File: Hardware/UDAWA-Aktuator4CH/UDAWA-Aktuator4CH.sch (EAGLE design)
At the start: 3 parts

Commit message: #3 to do list 1 sampai 5
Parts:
- added 5V, AC/DC1, AC/DC2, AC/DC3, AC/DC4, C1, C2, C3, C4, CH1, CH2, CH3, CH4, GND, NO1, NO3, RC1, RC2, RC3, RC4: (no value), con-wago-500:W237-102
- added F1, F2, F3, F4: (no value), fuse:19559
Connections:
- new net AC/DC1: AC/DC1-1.KL, CH1-2.KL
- new net AC/DC2: AC/DC2-1.KL, CH2-2.KL
- new net AC/DC3: AC/DC3-1.KL, CH3-2.KL
- new net AC/DC4: AC/DC4-1.KL, CH4-2.KL
- new net C1: C1-1.KL, U$1.IO27
- new net C2: C2-1.KL, U$1.IO26
- new net C3: C3-1.KL, U$1.IO25
- new net C4: C4-1.KL, U$1.IO33
- new net GND2: GND-1.KL, U$1.GND@2
- new net N$1: F1.2, RC1-2.KL
- new net N$3: F2.2, RC2-2.KL
- new net N$5: F3.2, RC3-2.KL
- new net N$7: F4.2, RC4-2.KL
- new net NO1: CH1-1.KL, NO1-1.KL
- new net NO2: CH2-1.KL, NO1-2.KL
- new net NO3: CH3-1.KL, NO3-1.KL
- new net NO4: CH4-1.KL, NO3-2.KL
- new net RC1: AC/DC1-2.KL, F1.1
- new net RC2: AC/DC2-2.KL, F2.1
- new net RC3: AC/DC3-2.KL, F3.1
- new net RC4: AC/DC4-2.KL, F4.1

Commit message: #3 perbaikan to do list 1sampai5
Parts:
- removed 5V, AC/DC2, AC/DC3, AC/DC4, C3, C4, RC3, RC4: (no value), con-wago-500:W237-102
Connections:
- removed net N$5: F3.2, RC3-2.KL
- removed net N$7: F4.2, RC4-2.KL
- removed net RC1: AC/DC1-2.KL, F1.1
- removed net RC2: AC/DC2-2.KL, F2.1
- removed net RC3: AC/DC3-2.KL, F3.1
- removed net RC4: AC/DC4-2.KL, F4.1
- new net -R1: AC/DC1-1.KL
- new net N$2: F2.2, RC1-1.KL
- new net N$4: F4.2, RC2-1.KL
- new net VCC: GND-2.KL, U$1.3V3
- new net ~R1: AC/DC1-2.KL, F1.1, F2.1, F3.1, F4.1
- net AC/DC1: no longer AC/DC1-1.KL
- net AC/DC2: no longer AC/DC2-1.KL
- net AC/DC3: no longer AC/DC3-1.KL
- net AC/DC4: no longer AC/DC4-1.KL
- net C2: now also C1-2.KL; no longer C2-1.KL
- net C3: now also C2-1.KL; no longer C3-1.KL
- net C4: now also C2-2.KL; no longer C4-1.KL
- net N$3: now also F3.2; no longer F2.2
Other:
- moved on the sheet: F1, F2, F3, F4

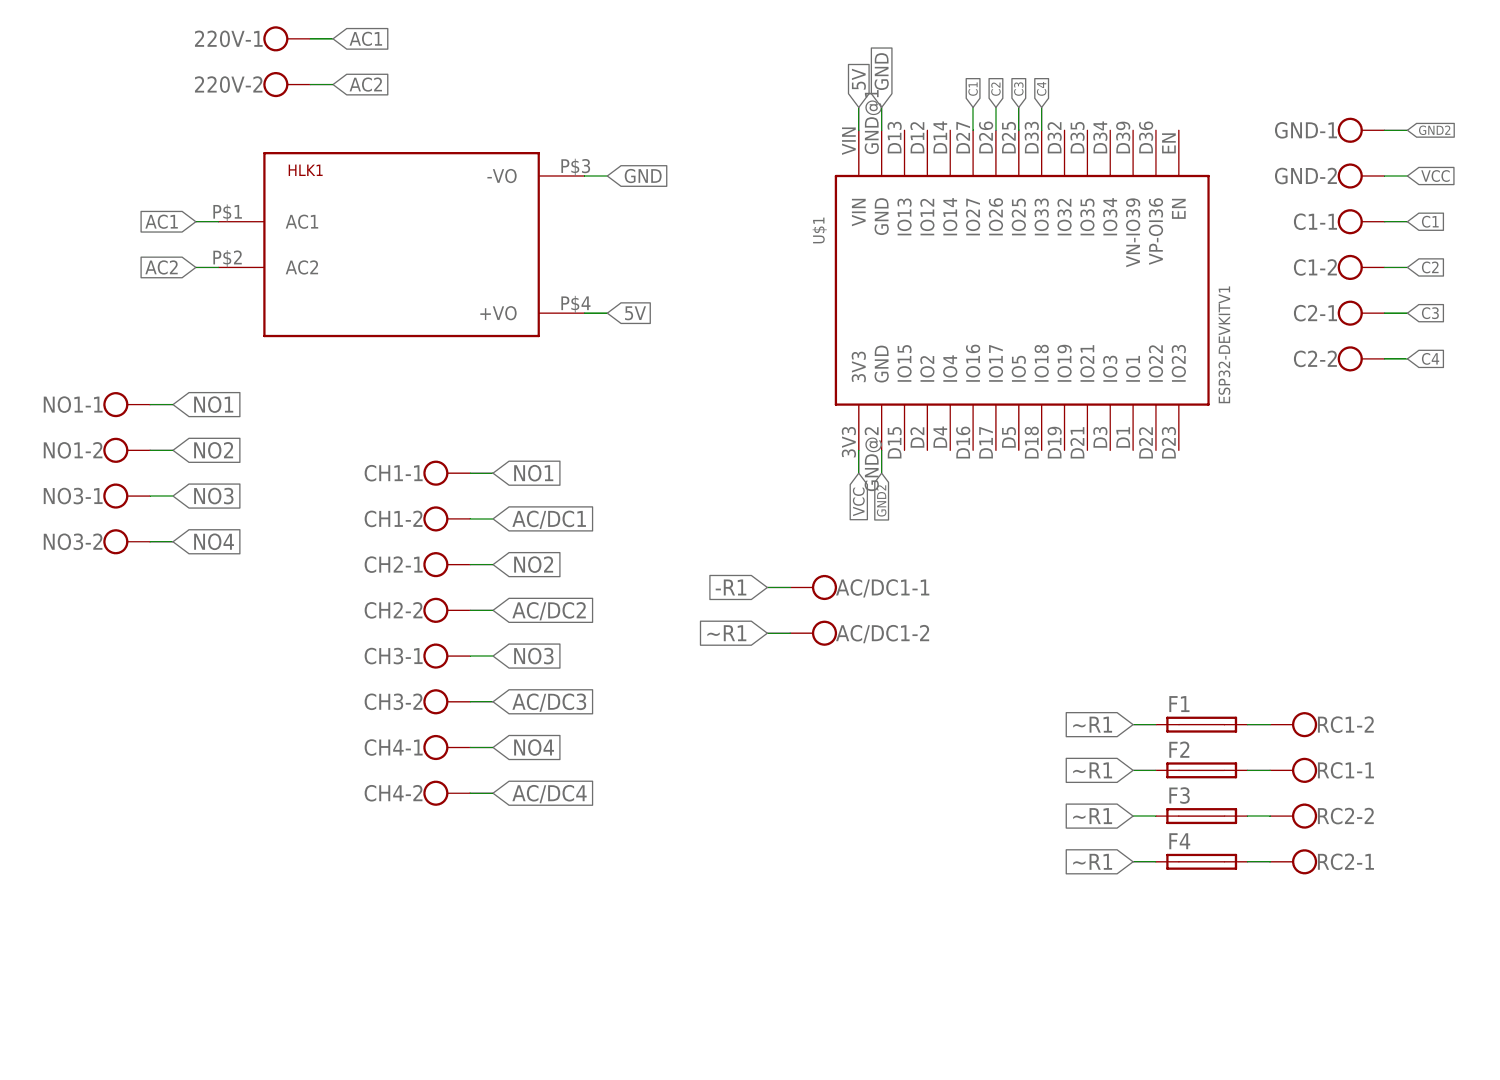
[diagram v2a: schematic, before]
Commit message: #3 wiring pada mode board dan pastikan penamaan setiap pin dan konektor dibuat dengan jelas dan rapi sesuai diagram.
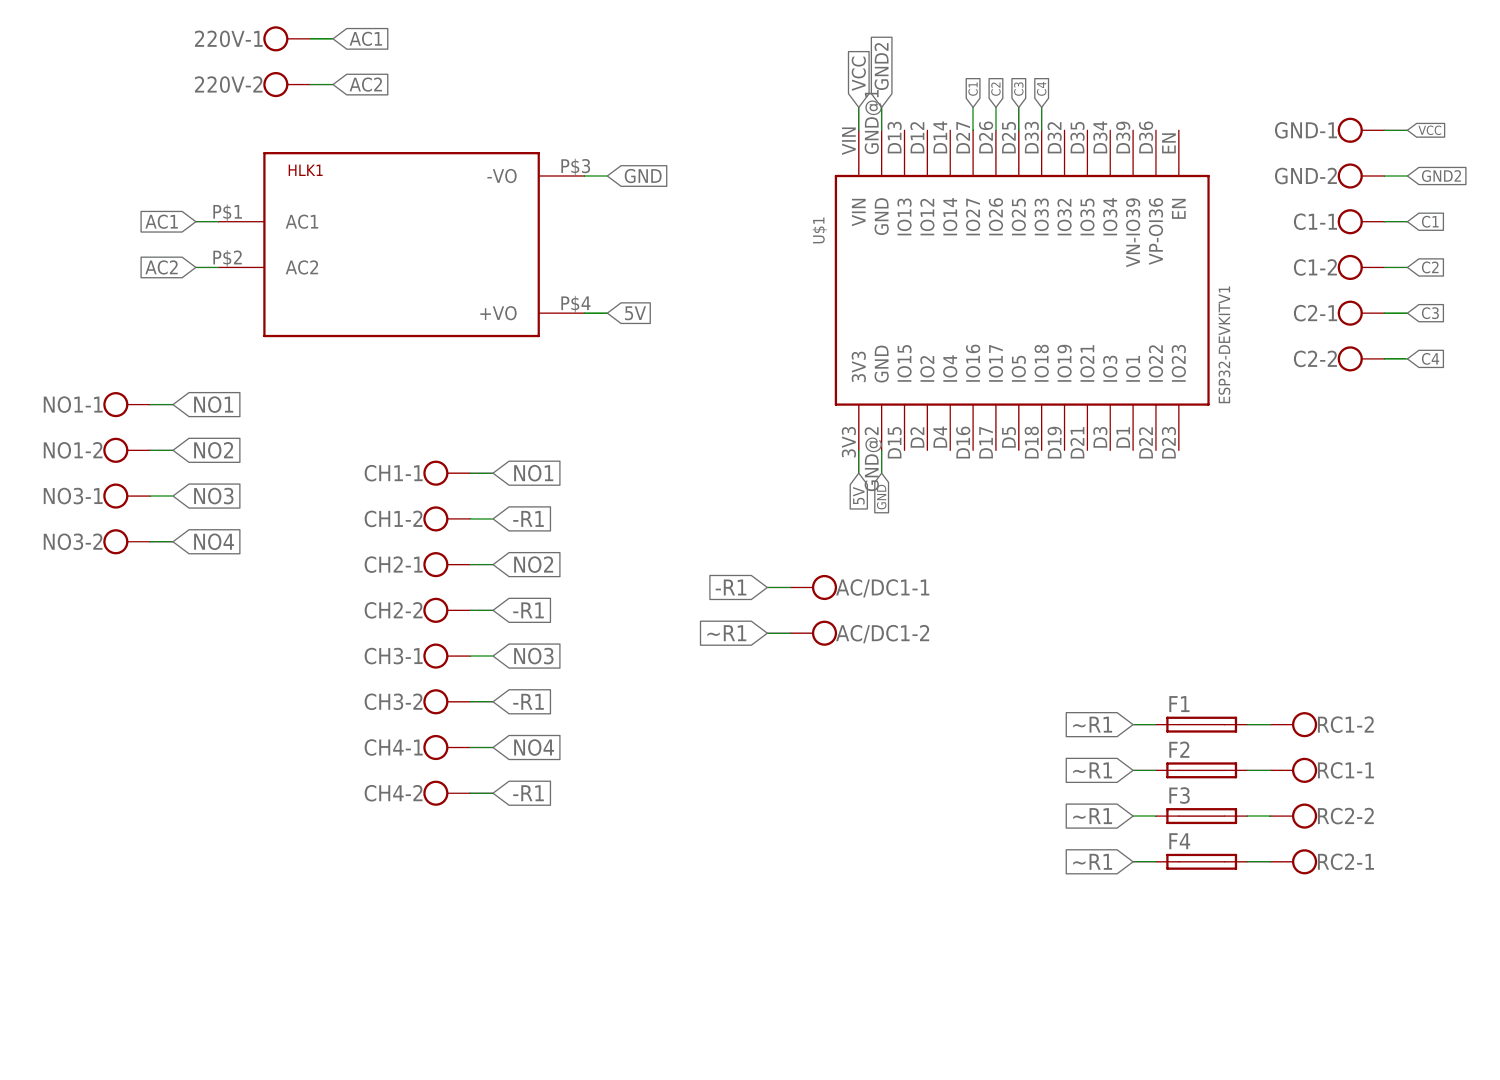
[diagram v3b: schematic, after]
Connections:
- removed net AC/DC1: CH1-2.KL
- removed net AC/DC2: CH2-2.KL
- removed net AC/DC3: CH3-2.KL
- removed net AC/DC4: CH4-2.KL
- net -R1: now also CH1-2.KL, CH2-2.KL, CH3-2.KL, CH4-2.KL
- net 5V: now also U$1.3V3; no longer U$1.VIN
- net GND: now also U$1.GND@2; no longer U$1.GND@1
- net GND2: now also GND-2.KL, U$1.GND@1; no longer GND-1.KL, U$1.GND@2
- net VCC: now also GND-1.KL, U$1.VIN; no longer GND-2.KL, U$1.3V3

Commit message: #3 list 8
masih belum lengkap  wiringnya karena kabelnya sudah mentok dan bakalan numpuk kalau dipaksakan
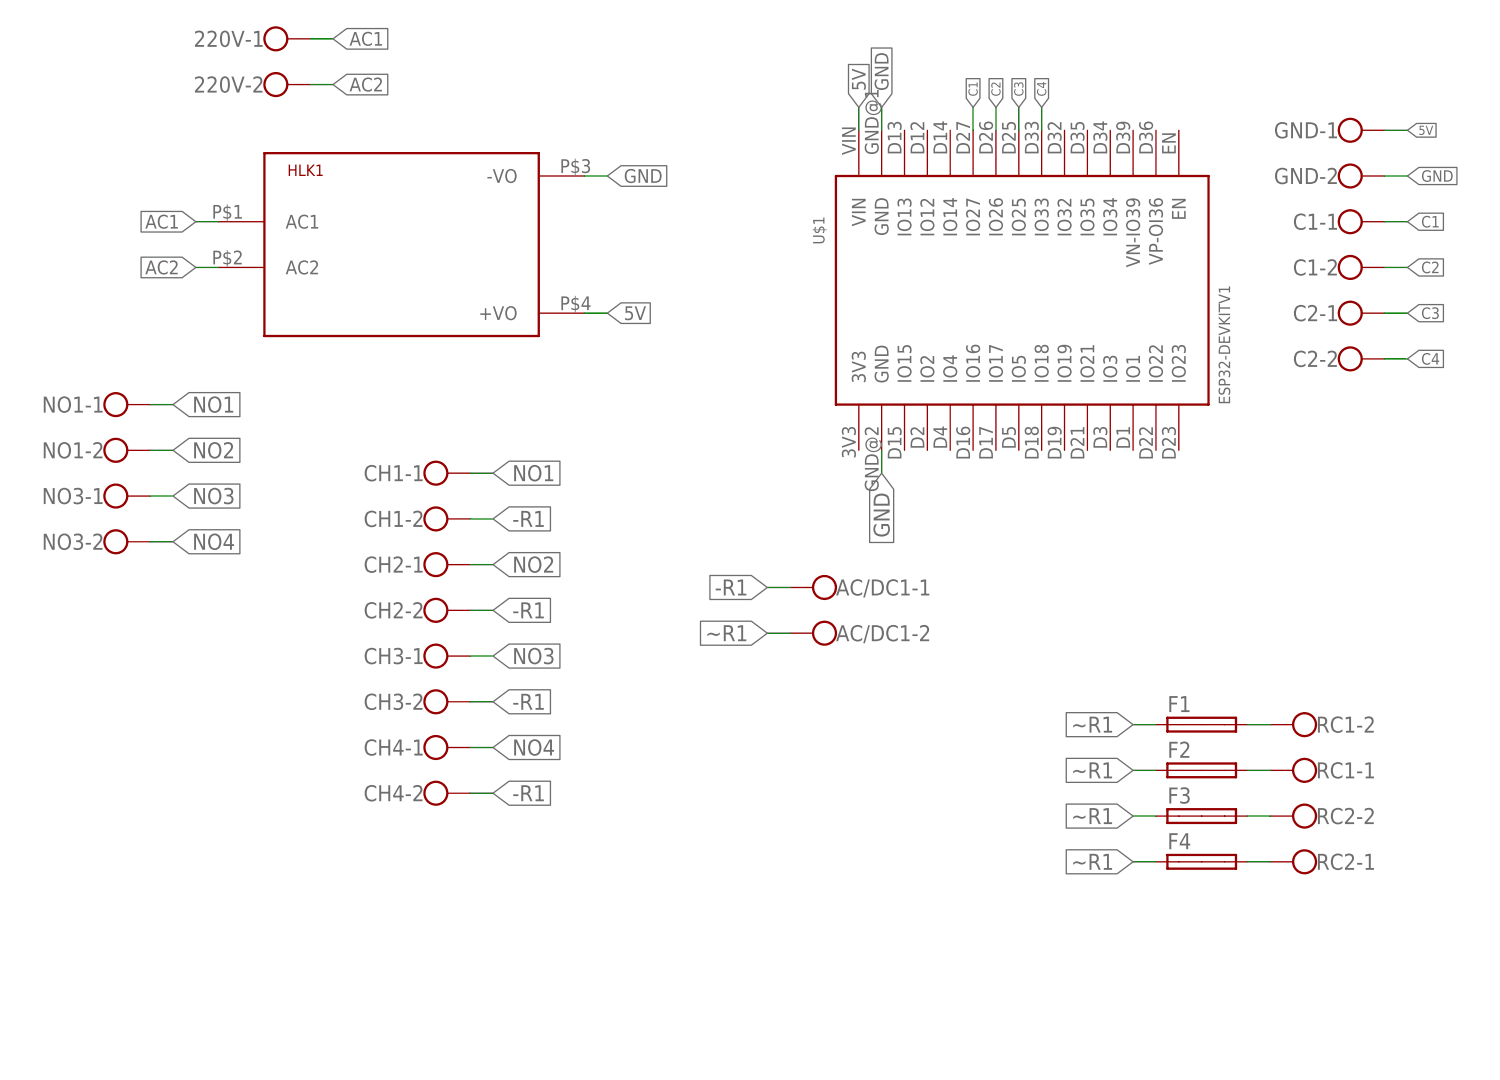
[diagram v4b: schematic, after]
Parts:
- F1, F2, F3, F4: device fuse:19559 -> fuse:SHK20L
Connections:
- removed net GND2: GND-2.KL, U$1.GND@1
- removed net VCC: GND-1.KL, U$1.VIN
- net 5V: now also GND-1.KL, U$1.VIN; no longer U$1.3V3
- net GND: now also GND-2.KL, U$1.GND@1
- net N$1: now also F1.2A; no longer F1.2
- net N$2: now also F2.2A; no longer F2.2
- net N$3: now also F3.2A; no longer F3.2
- net N$4: now also F4.2A; no longer F4.2
- net ~R1: now also F1.1A, F2.1A, F3.1A, F4.1A; no longer F1.1, F2.1, F3.1, F4.1
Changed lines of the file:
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@@
 <part name="RC1" library="con-wago-500" library_urn="urn:adsk.eagle:library:195" deviceset="W237-102" device="" package3d_urn="urn:adsk.eagle:package:10688/1"/>
 <part name="RC2" library="con-wago-500" library_urn="urn:adsk.eagle:library:195" deviceset="W237-102" device="" package3d_urn="urn:adsk.eagle:package:10688/1"/>
-<part name="F1" library="fuse" library_urn="urn:adsk.eagle:library:233" deviceset="19559" device="" package3d_urn="urn:adsk.eagle:package:14056/1"/>
-<part name="F2" library="fuse" library_urn="urn:adsk.eagle:library:233" deviceset="19559" device="" package3d_urn="urn:adsk.eagle:package:14056/1"/>
-<part name="F3" library="fuse" library_urn="urn:adsk.eagle:library:233" deviceset="19559" device="" package3d_urn="urn:adsk.eagle:package:14056/1"/>
-<part name="F4" library="fuse" library_urn="urn:adsk.eagle:library:233" deviceset="19559" device="" package3d_urn="urn:adsk.eagle:package:14056/1"/>
+<part name="F1" library="fuse" library_urn="urn:adsk.eagle:library:233" deviceset="SHK20L" device="" package3d_urn="urn:adsk.eagle:package:14071/1"/>
+<part name="F2" library="fuse" library_urn="urn:adsk.eagle:library:233" deviceset="SHK20L" device="" package3d_urn="urn:adsk.eagle:package:14071/1"/>
+<part name="F3" library="fuse" library_urn="urn:adsk.eagle:library:233" deviceset="SHK20L" device="" package3d_urn="urn:adsk.eagle:package:14071/1"/>
+<part name="F4" library="fuse" library_urn="urn:adsk.eagle:library:233" deviceset="SHK20L" device="" package3d_urn="urn:adsk.eagle:package:14071/1"/>
 </parts>
 <sheets>
@@
 <attribute name="NAME" x="73.66" y="-61.849" size="1.778" layer="95"/>
 </instance>
-<instance part="F1" gate="1" x="60.96" y="-50.8" smashed="yes">
+<instance part="F1" gate="G$1" x="60.96" y="-50.8" smashed="yes">
 <attribute name="NAME" x="57.15" y="-49.403" size="1.778" layer="95"/>
 <attribute name="VALUE" x="57.15" y="-53.721" size="1.778" layer="96"/>
 </instance>
-<instance part="F2" gate="1" x="60.96" y="-55.88" smashed="yes">
+<instance part="F2" gate="G$1" x="60.96" y="-55.88" smashed="yes">
 <attribute name="NAME" x="57.15" y="-54.483" size="1.778" layer="95"/>
 <attribute name="VALUE" x="57.15" y="-58.801" size="1.778" layer="96"/>
 </instance>
-<instance part="F3" gate="1" x="60.96" y="-60.96" smashed="yes">
+<instance part="F3" gate="G$1" x="60.96" y="-60.96" smashed="yes">
 <attribute name="NAME" x="57.15" y="-59.563" size="1.778" layer="95"/>
 <attribute name="VALUE" x="57.15" y="-63.881" size="1.778" layer="96"/>
 </instance>
-<instance part="F4" gate="1" x="60.96" y="-66.04" smashed="yes">
+<instance part="F4" gate="G$1" x="60.96" y="-66.04" smashed="yes">
 <attribute name="NAME" x="57.15" y="-64.643" size="1.778" layer="95"/>
 <attribute name="VALUE" x="57.15" y="-68.961" size="1.778" layer="96"/>
@@
 </segment>
 <segment>
+<pinref part="U$1" gate="G$1" pin="GND@1"/>
+<wire x1="25.4" y1="15.24" x2="25.4" y2="17.78" width="0.1524" layer="91"/>
+<label x="25.4" y="17.78" size="1.524" layer="95" rot="R90" xref="yes"/>
+</segment>
+<segment>
+<pinref part="GND" gate="-2" pin="KL"/>
+<wire x1="81.28" y1="10.16" x2="83.82" y2="10.16" width="0.1524" layer="91"/>
+<label x="83.82" y="10.16" size="1.27" layer="95" xref="yes"/>
+</segment>
+<segment>
 <pinref part="U$1" gate="G$1" pin="GND@2"/>
 <wire x1="25.4" y1="-20.32" x2="25.4" y2="-22.86" width="0.1524" layer="91"/>
-<label x="25.4" y="-22.86" size="1.016" layer="95" rot="R270" xref="yes"/>
+<label x="25.4" y="-22.86" size="1.778" layer="95" rot="R270" xref="yes"/>
 </segment>
 </net>
@@
 </segment>
 <segment>
-<pinref part="U$1" gate="G$1" pin="3V3"/>
-<wire x1="22.86" y1="-20.32" x2="22.86" y2="-22.86" width="0.1524" layer="91"/>
-<label x="22.86" y="-22.86" size="1.27" layer="95" rot="R270" xref="yes"/>
+<pinref part="U$1" gate="G$1" pin="VIN"/>
+<wire x1="22.86" y1="15.24" x2="22.86" y2="17.78" width="0.1524" layer="91"/>
+<label x="22.86" y="17.78" size="1.524" layer="95" rot="R90" xref="yes"/>
+</segment>
+<segment>
+<pinref part="GND" gate="-1" pin="KL"/>
+<wire x1="81.28" y1="15.24" x2="83.82" y2="15.24" width="0.1524" layer="91"/>
+<label x="83.82" y="15.24" size="1.016" layer="95" xref="yes"/>
 </segment>
 </net>
@@
 <segment>
 <pinref part="RC1" gate="-2" pin="KL"/>
-<pinref part="F1" gate="1" pin="2"/>
+<pinref part="F1" gate="G$1" pin="2A"/>
 <wire x1="66.04" y1="-50.8" x2="68.58" y2="-50.8" width="0.1524" layer="91"/>
 </segment>
 </net>
-<net name="GND2" class="0">
-<segment>
-<pinref part="U$1" gate="G$1" pin="GND@1"/>
-<wire x1="25.4" y1="15.24" x2="25.4" y2="17.78" width="0.1524" layer="91"/>
-<label x="25.4" y="17.78" size="1.524" layer="95" rot="R90" xref="yes"/>
-</segment>
-<segment>
-<pinref part="GND" gate="-2" pin="KL"/>
-<wire x1="81.28" y1="10.16" x2="83.82" y2="10.16" width="0.1524" layer="91"/>
-<label x="83.82" y="10.16" size="1.27" layer="95" xref="yes"/>
-</segment>
-</net>
-<net name="VCC" class="0">
-<segment>
-<pinref part="U$1" gate="G$1" pin="VIN"/>
-<wire x1="22.86" y1="15.24" x2="22.86" y2="17.78" width="0.1524" layer="91"/>
-<label x="22.86" y="17.78" size="1.524" layer="95" rot="R90" xref="yes"/>
-</segment>
-<segment>
-<pinref part="GND" gate="-1" pin="KL"/>
-<wire x1="81.28" y1="15.24" x2="83.82" y2="15.24" width="0.1524" layer="91"/>
-<label x="83.82" y="15.24" size="1.016" layer="95" xref="yes"/>
-</segment>
-</net>
 <net name="N$2" class="0">
 <segment>
 <pinref part="RC1" gate="-1" pin="KL"/>
-<pinref part="F2" gate="1" pin="2"/>
+<pinref part="F2" gate="G$1" pin="2A"/>
 <wire x1="66.04" y1="-55.88" x2="68.58" y2="-55.88" width="0.1524" layer="91"/>
 </segment>
@@
 <net name="N$3" class="0">
 <segment>
-<pinref part="F3" gate="1" pin="2"/>
+<pinref part="F3" gate="G$1" pin="2A"/>
 <pinref part="RC2" gate="-2" pin="KL"/>
 <wire x1="66.04" y1="-60.96" x2="68.58" y2="-60.96" width="0.1524" layer="91"/>
@@
 <segment>
 <pinref part="RC2" gate="-1" pin="KL"/>
-<pinref part="F4" gate="1" pin="2"/>
+<pinref part="F4" gate="G$1" pin="2A"/>
 <wire x1="68.58" y1="-66.04" x2="66.04" y2="-66.04" width="0.1524" layer="91"/>
 </segment>
@@
 </segment>
 <segment>
-<pinref part="F1" gate="1" pin="1"/>
+<pinref part="F1" gate="G$1" pin="1A"/>
 <wire x1="55.88" y1="-50.8" x2="53.34" y2="-50.8" width="0.1524" layer="91"/>
 <label x="53.34" y="-50.8" size="1.778" layer="95" rot="MR0" xref="yes"/>
 </segment>
 <segment>
-<pinref part="F2" gate="1" pin="1"/>
+<pinref part="F2" gate="G$1" pin="1A"/>
 <wire x1="55.88" y1="-55.88" x2="53.34" y2="-55.88" width="0.1524" layer="91"/>
 <label x="53.34" y="-55.88" size="1.778" layer="95" rot="MR0" xref="yes"/>
 </segment>
 <segment>
-<pinref part="F3" gate="1" pin="1"/>
+<pinref part="F3" gate="G$1" pin="1A"/>
 <wire x1="55.88" y1="-60.96" x2="53.34" y2="-60.96" width="0.1524" layer="91"/>
 <label x="53.34" y="-60.96" size="1.778" layer="95" rot="MR0" xref="yes"/>
 </segment>
 <segment>
-<pinref part="F4" gate="1" pin="1"/>
+<pinref part="F4" gate="G$1" pin="1A"/>
 <wire x1="55.88" y1="-66.04" x2="53.34" y2="-66.04" width="0.1524" layer="91"/>
 <label x="53.34" y="-66.04" size="1.778" layer="95" rot="MR0" xref="yes"/>
